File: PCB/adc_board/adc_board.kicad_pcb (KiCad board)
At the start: 4 copper layers, 7 parts, among them U1 MAX6070BAUT33T

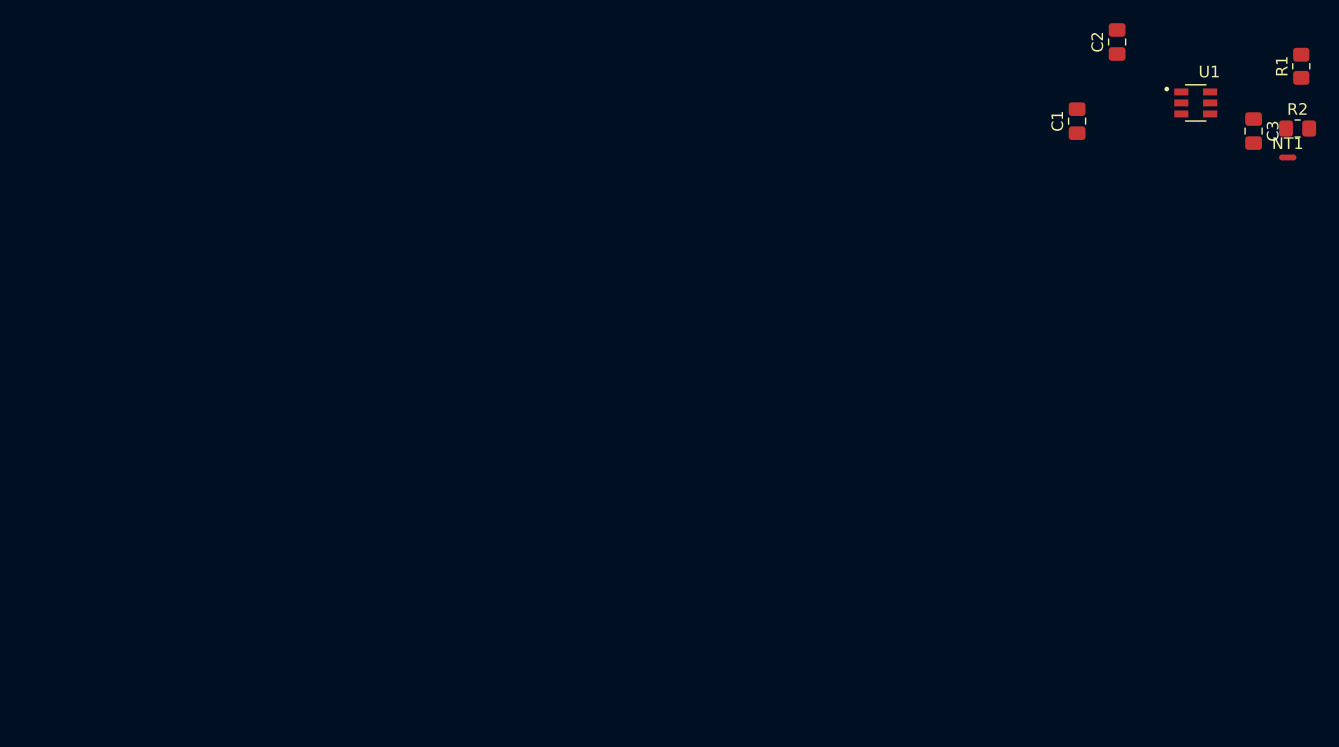
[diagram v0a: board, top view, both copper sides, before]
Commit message: Finished layout for adc board
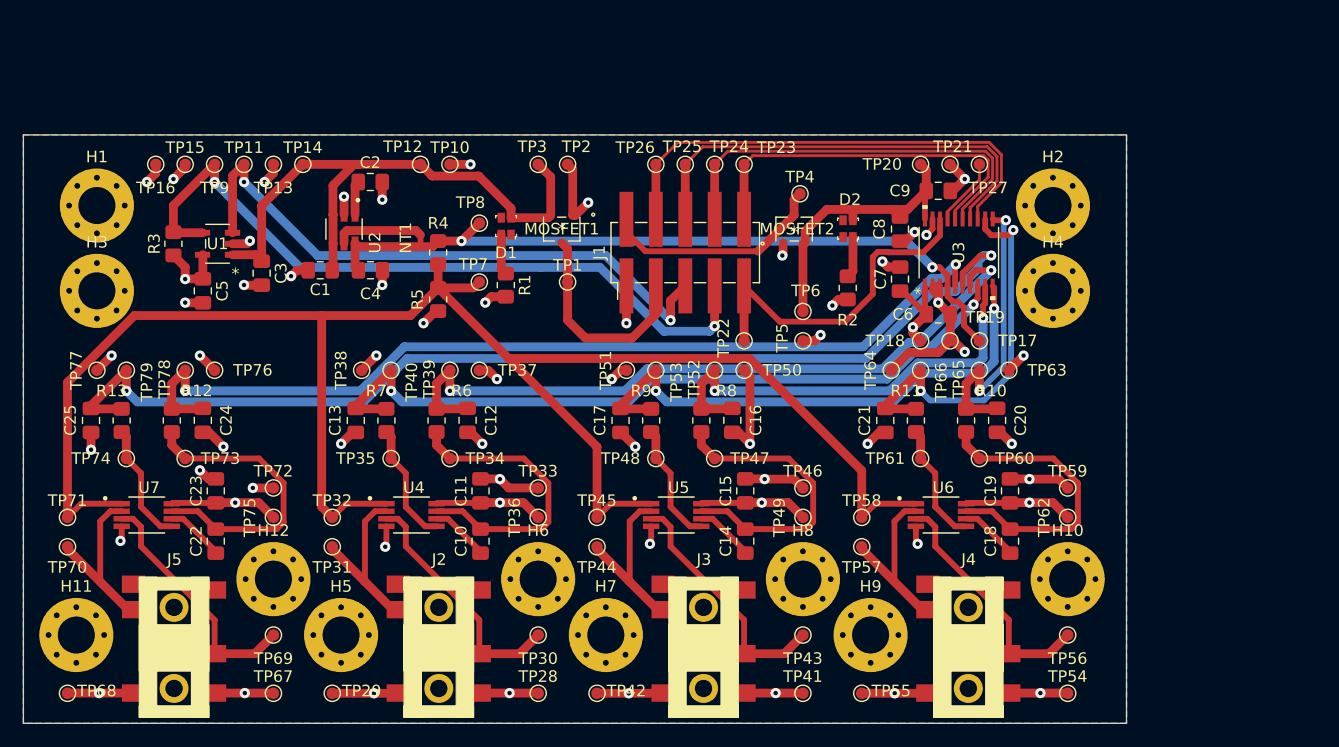
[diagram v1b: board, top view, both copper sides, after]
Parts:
- added C10: 10nF, Capacitor_SMD:C_0805_2012Metric_Pad1.18x1.45mm_HandSolder, F.Cu at (89.0, 124.0)
- added C11: 0.1uF, Capacitor_SMD:C_0805_2012Metric_Pad1.18x1.45mm_HandSolder, F.Cu at (89.0, 119.6)
- added C12: 0.1uF, Capacitor_SMD:C_0805_2012Metric_Pad1.18x1.45mm_HandSolder, F.Cu at (87.9, 113.5)
- added C13: 0.1uF, Capacitor_SMD:C_0805_2012Metric_Pad1.18x1.45mm_HandSolder, F.Cu at (78.2, 113.6)
- added C14: 10nF, Capacitor_SMD:C_0805_2012Metric_Pad1.18x1.45mm_HandSolder, F.Cu at (111.9, 124.0)
- added C15: 0.1uF, Capacitor_SMD:C_0805_2012Metric_Pad1.18x1.45mm_HandSolder, F.Cu at (111.9, 119.6)
- added C16: 0.1uF, Capacitor_SMD:C_0805_2012Metric_Pad1.18x1.45mm_HandSolder, F.Cu at (110.7, 113.5)
- added C17: 0.1uF, Capacitor_SMD:C_0805_2012Metric_Pad1.18x1.45mm_HandSolder, F.Cu at (101.1, 113.6)
- added C18: 10nF, Capacitor_SMD:C_0805_2012Metric_Pad1.18x1.45mm_HandSolder, F.Cu at (134.7, 124.0)
- added C19: 0.1uF, Capacitor_SMD:C_0805_2012Metric_Pad1.18x1.45mm_HandSolder, F.Cu at (134.7, 119.6)
- added C20: 0.1uF, Capacitor_SMD:C_0805_2012Metric_Pad1.18x1.45mm_HandSolder, F.Cu at (133.6, 113.5)
- added C21: 0.1uF, Capacitor_SMD:C_0805_2012Metric_Pad1.18x1.45mm_HandSolder, F.Cu at (124.0, 113.6)
- added C22: 10nF, Capacitor_SMD:C_0805_2012Metric_Pad1.18x1.45mm_HandSolder, F.Cu at (66.1, 124.0)
- added C23: 0.1uF, Capacitor_SMD:C_0805_2012Metric_Pad1.18x1.45mm_HandSolder, F.Cu at (66.1, 119.6)
- added C24: 0.1uF, Capacitor_SMD:C_0805_2012Metric_Pad1.18x1.45mm_HandSolder, F.Cu at (65.0, 113.5)
- added C25: 0.1uF, Capacitor_SMD:C_0805_2012Metric_Pad1.18x1.45mm_HandSolder, F.Cu at (55.4, 113.6)
- added C4: 0.1uF, Capacitor_SMD:C_0805_2012Metric_Pad1.18x1.45mm_HandSolder, F.Cu at (79.5, 100.6)
- added C5: 10uF, Capacitor_SMD:C_0805_2012Metric_Pad1.18x1.45mm_HandSolder, F.Cu at (65.0, 102.4)
- added C6: 0.1uF, Capacitor_SMD:C_0805_2012Metric_Pad1.18x1.45mm_HandSolder, F.Cu at (128.5, 104.4)
- added C7: 10uF, Capacitor_SMD:C_0805_2012Metric_Pad1.18x1.45mm_HandSolder, F.Cu at (125.2, 101.3)
- added C8: 10uF, Capacitor_SMD:C_0805_2012Metric_Pad1.18x1.45mm_HandSolder, F.Cu at (125.2, 97.0)
- added C9: 0.1uF, Capacitor_SMD:C_0805_2012Metric_Pad1.18x1.45mm_HandSolder, F.Cu at (128.5, 93.7)
- added D1: LTST-C19HE1WT, digikey-footprints:LED_Dual0603, F.Cu at (91.2, 96.8)
- added D2: LTST-C19HE1WT, digikey-footprints:LED_Dual0603, F.Cu at (120.7, 97.0)
- added H1: MountingHole, MountingHole:MountingHole_3.2mm_M3_Pad_Via, F.Cu at (55.9, 95.0)
- added H10: MountingHole, MountingHole:MountingHole_3.2mm_M3_Pad_Via, F.Cu at (139.7, 127.3)
- added H11: MountingHole, MountingHole:MountingHole_3.2mm_M3_Pad_Via, F.Cu at (54.1, 132.1)
- added H12: MountingHole, MountingHole:MountingHole_3.2mm_M3_Pad_Via, F.Cu at (71.1, 127.3)
- added H2: MountingHole, MountingHole:MountingHole_3.2mm_M3_Pad_Via, F.Cu at (138.4, 95.0)
- added H3: MountingHole, MountingHole:MountingHole_3.2mm_M3_Pad_Via, F.Cu at (55.9, 102.4)
- added H4: MountingHole, MountingHole:MountingHole_3.2mm_M3_Pad_Via, F.Cu at (138.4, 102.4)
- added H5: MountingHole, MountingHole:MountingHole_3.2mm_M3_Pad_Via, F.Cu at (77.0, 132.1)
- added H6: MountingHole, MountingHole:MountingHole_3.2mm_M3_Pad_Via, F.Cu at (94.0, 127.3)
- added H7: MountingHole, MountingHole:MountingHole_3.2mm_M3_Pad_Via, F.Cu at (99.8, 132.1)
- added H8: MountingHole, MountingHole:MountingHole_3.2mm_M3_Pad_Via, F.Cu at (116.8, 127.3)
- added H9: MountingHole, MountingHole:MountingHole_3.2mm_M3_Pad_Via, F.Cu at (122.7, 132.1)
- added J1: Conn_02x05_Counter_Clockwise, 2x5header:PinHeader_2x05_P2.54mm_Vertical_SMD, F.Cu at (106.7, 99.1)
- added J2: 54-00177, 54-00177:54-00177, F.Cu at (88.9, 139.2)
- added J3: 54-00177, 54-00177:54-00177, F.Cu at (111.8, 139.2)
- added J4: 54-00177, 54-00177:54-00177, F.Cu at (134.6, 139.2)
- added J5: 54-00177, 54-00177:54-00177, F.Cu at (66.0, 139.2)
- added MOSFET1: SSM3J332R, ul_SSM3J332R:SSM3J332R, F.Cu at (96.0, 97.0)
- added MOSFET2: SSM3J332R, ul_SSM3J332R:SSM3J332R, F.Cu at (116.1, 97.0)
- added R10: 100R, Resistor_SMD:R_0805_2012Metric_Pad1.20x1.40mm_HandSolder, F.Cu at (130.9, 113.6)
- added R11: 100R, Resistor_SMD:R_0805_2012Metric_Pad1.20x1.40mm_HandSolder, F.Cu at (126.6, 113.6)
- added R12: 100R, Resistor_SMD:R_0805_2012Metric_Pad1.20x1.40mm_HandSolder, F.Cu at (62.3, 113.6)
- added R13: 100R, Resistor_SMD:R_0805_2012Metric_Pad1.20x1.40mm_HandSolder, F.Cu at (58.0, 113.6)
- added R3: 10K 0.5%, Resistor_SMD:R_0805_2012Metric_Pad1.20x1.40mm_HandSolder, F.Cu at (62.5, 98.3)
- added R4: 10K 0.5%, Resistor_SMD:R_0805_2012Metric_Pad1.20x1.40mm_HandSolder, F.Cu at (85.3, 99.1)
- added R5: 10K 0.5%, Resistor_SMD:R_0805_2012Metric_Pad1.20x1.40mm_HandSolder, F.Cu at (85.3, 103.1)
- added R6: 100R, Resistor_SMD:R_0805_2012Metric_Pad1.20x1.40mm_HandSolder, F.Cu at (85.2, 113.6)
- added R7: 100R, Resistor_SMD:R_0805_2012Metric_Pad1.20x1.40mm_HandSolder, F.Cu at (80.9, 113.6)
- added R8: 100R, Resistor_SMD:R_0805_2012Metric_Pad1.20x1.40mm_HandSolder, F.Cu at (108.1, 113.6)
- added R9: 100R, Resistor_SMD:R_0805_2012Metric_Pad1.20x1.40mm_HandSolder, F.Cu at (103.7, 113.6)
- added TP1: 3V3, TestPoint:TestPoint_Pad_D1.0mm, F.Cu at (96.5, 101.6)
- added TP10: GND, TestPoint:TestPoint_Pad_D1.0mm, F.Cu at (86.4, 91.4)
- added TP11: ENABLE, TestPoint:TestPoint_Pad_D1.0mm, F.Cu at (68.6, 91.4)
- added TP12: 5V_PROT, TestPoint:TestPoint_Pad_D1.0mm, F.Cu at (83.8, 91.4)
- added TP13: GND, TestPoint:TestPoint_Pad_D1.0mm, F.Cu at (71.1, 91.4)
- added TP14: 5V_PROT, TestPoint:TestPoint_Pad_D1.0mm, F.Cu at (73.7, 91.4)
- added TP15: AVDD, TestPoint:TestPoint_Pad_D1.0mm, F.Cu at (63.5, 91.4)
- added TP16: GND, TestPoint:TestPoint_Pad_D1.0mm, F.Cu at (61.0, 91.4)
- added TP17: 3V3_REF, TestPoint:TestPoint_Pad_D1.0mm, F.Cu at (132.1, 106.7)
- added TP18: AVDD, TestPoint:TestPoint_Pad_D1.0mm, F.Cu at (127.0, 106.7)
- added TP19: GND, TestPoint:TestPoint_Pad_D1.0mm, F.Cu at (129.5, 106.7)
- added TP2: GND, TestPoint:TestPoint_Pad_D1.0mm, F.Cu at (96.5, 91.4)
- added TP20: DVDD, TestPoint:TestPoint_Pad_D1.0mm, F.Cu at (127.0, 91.4)
- added TP21: GND, TestPoint:TestPoint_Pad_D1.0mm, F.Cu at (129.5, 91.4)
- added TP22: CLK, TestPoint:TestPoint_Pad_D1.0mm, F.Cu at (111.8, 106.7)
- added TP23: MISO, TestPoint:TestPoint_Pad_D1.0mm, F.Cu at (111.8, 91.4)
- added TP24: MOSI, TestPoint:TestPoint_Pad_D1.0mm, F.Cu at (109.2, 91.4)
- added TP25: SCK, TestPoint:TestPoint_Pad_D1.0mm, F.Cu at (106.7, 91.4)
- added TP26: CS, TestPoint:TestPoint_Pad_D1.0mm, F.Cu at (104.1, 91.4)
- added TP27: IRQ, TestPoint:TestPoint_Pad_D1.0mm, F.Cu at (132.1, 91.4)
- added TP28: VDD, TestPoint:TestPoint_Pad_D1.0mm, F.Cu at (94.0, 137.1)
- added TP29: GND, TestPoint:TestPoint_Pad_D1.0mm, F.Cu at (76.2, 137.1)
- added TP3: 5V_PROT, TestPoint:TestPoint_Pad_D1.0mm, F.Cu at (94.0, 91.4)
- added TP30: BR+, TestPoint:TestPoint_Pad_D1.0mm, F.Cu at (94.0, 132.1)
- added TP31: BR-, TestPoint:TestPoint_Pad_D1.0mm, F.Cu at (76.2, 124.5)
- added TP32: 1V65, TestPoint:TestPoint_Pad_D1.0mm, F.Cu at (76.2, 121.9)
- added TP33: GND, TestPoint:TestPoint_Pad_D1.0mm, F.Cu at (94.0, 119.4)
- added TP34: AMP+, TestPoint:TestPoint_Pad_D1.0mm, F.Cu at (86.4, 116.8)
- added TP35: AMP-, TestPoint:TestPoint_Pad_D1.0mm, F.Cu at (81.3, 116.8)
- added TP36: VDD, TestPoint:TestPoint_Pad_D1.0mm, F.Cu at (94.0, 121.9)
- added TP37: GND, TestPoint:TestPoint_Pad_D1.0mm, F.Cu at (88.9, 109.2)
- added TP38: GND, TestPoint:TestPoint_Pad_D1.0mm, F.Cu at (78.7, 109.2)
- added TP39: DIFF+, TestPoint:TestPoint_Pad_D1.0mm, F.Cu at (86.4, 109.2)
- added TP4: 3V3, TestPoint:TestPoint_Pad_D1.0mm, F.Cu at (116.6, 94.0)
- added TP40: DIFF-, TestPoint:TestPoint_Pad_D1.0mm, F.Cu at (81.3, 109.2)
- added TP41: VDD, TestPoint:TestPoint_Pad_D1.0mm, F.Cu at (116.8, 137.1)
- added TP42: GND, TestPoint:TestPoint_Pad_D1.0mm, F.Cu at (99.1, 137.1)
- added TP43: BR+, TestPoint:TestPoint_Pad_D1.0mm, F.Cu at (116.8, 132.1)
- added TP44: BR-, TestPoint:TestPoint_Pad_D1.0mm, F.Cu at (99.1, 124.5)
- added TP45: 1V65, TestPoint:TestPoint_Pad_D1.0mm, F.Cu at (99.1, 121.9)
- added TP46: GND, TestPoint:TestPoint_Pad_D1.0mm, F.Cu at (116.8, 119.4)
- added TP47: AMP+, TestPoint:TestPoint_Pad_D1.0mm, F.Cu at (109.2, 116.8)
- added TP48: AMP-, TestPoint:TestPoint_Pad_D1.0mm, F.Cu at (104.1, 116.8)
- added TP49: VDD, TestPoint:TestPoint_Pad_D1.0mm, F.Cu at (116.8, 121.9)
- added TP5: GND, TestPoint:TestPoint_Pad_D1.0mm, F.Cu at (116.8, 106.7)
- added TP50: GND, TestPoint:TestPoint_Pad_D1.0mm, F.Cu at (111.8, 109.2)
- added TP51: GND, TestPoint:TestPoint_Pad_D1.0mm, F.Cu at (101.6, 109.2)
- added TP52: DIFF+, TestPoint:TestPoint_Pad_D1.0mm, F.Cu at (109.2, 109.2)
- added TP53: DIFF-, TestPoint:TestPoint_Pad_D1.0mm, F.Cu at (104.1, 109.2)
- added TP54: VDD, TestPoint:TestPoint_Pad_D1.0mm, F.Cu at (139.7, 137.1)
- added TP55: GND, TestPoint:TestPoint_Pad_D1.0mm, F.Cu at (121.9, 137.1)
- added TP56: BR+, TestPoint:TestPoint_Pad_D1.0mm, F.Cu at (139.7, 132.1)
- added TP57: BR-, TestPoint:TestPoint_Pad_D1.0mm, F.Cu at (121.9, 124.5)
- added TP58: 1V65, TestPoint:TestPoint_Pad_D1.0mm, F.Cu at (121.9, 121.9)
- added TP59: GND, TestPoint:TestPoint_Pad_D1.0mm, F.Cu at (139.7, 119.4)
- added TP6: 3V3_PROT, TestPoint:TestPoint_Pad_D1.0mm, F.Cu at (116.8, 104.1)
- added TP60: AMP+, TestPoint:TestPoint_Pad_D1.0mm, F.Cu at (132.1, 116.8)
- added TP61: AMP-, TestPoint:TestPoint_Pad_D1.0mm, F.Cu at (127.0, 116.8)
- added TP62: VDD, TestPoint:TestPoint_Pad_D1.0mm, F.Cu at (139.7, 121.9)
- added TP63: GND, TestPoint:TestPoint_Pad_D1.0mm, F.Cu at (134.6, 109.2)
- added TP64: GND, TestPoint:TestPoint_Pad_D1.0mm, F.Cu at (124.5, 109.2)
- added TP65: DIFF+, TestPoint:TestPoint_Pad_D1.0mm, F.Cu at (132.1, 109.2)
- added TP66: DIFF-, TestPoint:TestPoint_Pad_D1.0mm, F.Cu at (127.0, 109.2)
- added TP67: VDD, TestPoint:TestPoint_Pad_D1.0mm, F.Cu at (71.1, 137.1)
- added TP68: GND, TestPoint:TestPoint_Pad_D1.0mm, F.Cu at (53.3, 137.1)
- added TP69: BR+, TestPoint:TestPoint_Pad_D1.0mm, F.Cu at (71.1, 132.1)
- added TP7: 1V65_REF, TestPoint:TestPoint_Pad_D1.0mm, F.Cu at (88.9, 101.6)
- added TP70: BR-, TestPoint:TestPoint_Pad_D1.0mm, F.Cu at (53.3, 124.5)
- added TP71: 1V65, TestPoint:TestPoint_Pad_D1.0mm, F.Cu at (53.3, 121.9)
- added TP72: GND, TestPoint:TestPoint_Pad_D1.0mm, F.Cu at (71.1, 119.4)
- added TP73: AMP+, TestPoint:TestPoint_Pad_D1.0mm, F.Cu at (63.5, 116.8)
- added TP74: AMP-, TestPoint:TestPoint_Pad_D1.0mm, F.Cu at (58.4, 116.8)
- added TP75: VDD, TestPoint:TestPoint_Pad_D1.0mm, F.Cu at (71.1, 121.9)
- added TP76: GND, TestPoint:TestPoint_Pad_D1.0mm, F.Cu at (66.0, 109.2)
- added TP77: GND, TestPoint:TestPoint_Pad_D1.0mm, F.Cu at (55.9, 109.2)
- added TP78: DIFF+, TestPoint:TestPoint_Pad_D1.0mm, F.Cu at (63.5, 109.2)
- added TP79: DIFF-, TestPoint:TestPoint_Pad_D1.0mm, F.Cu at (58.4, 109.2)
- added TP8: 3V3_REF, TestPoint:TestPoint_Pad_D1.0mm, F.Cu at (88.9, 96.5)
- added TP9: PGOOD, TestPoint:TestPoint_Pad_D1.0mm, F.Cu at (66.0, 91.4)
- added U2: MAX6070BAUT33T, MAX6070BAUT33T:SOT95P280X145-6N, F.Cu at (77.2, 97.0)
- added U3: MCP3564-E_ST, ‎MCP3564-E-ST:MCP3564-E&slash_ST, F.Cu at (130.3, 99.1)
- added U4: MAX4209HAUA, MAX4209HAUA:SOP65P490X110-8N, F.Cu at (83.0, 121.7)
- added U5: MAX4209HAUA, MAX4209HAUA:SOP65P490X110-8N, F.Cu at (105.9, 121.7)
- added U6: MAX4209HAUA, MAX4209HAUA:SOP65P490X110-8N, F.Cu at (128.8, 121.7)
- added U7: MAX4209HAUA, MAX4209HAUA:SOP65P490X110-8N, F.Cu at (60.2, 121.7)
- C3: value 0.1uF -> 10uF
- R1, R2: value 10K -> 100R
- U1: value MAX6070BAUT33T -> MCP1755T-3302E_OT; footprint MAX6070BAUT33T:SOT95P280X145-6N -> ul_MCP1755T-3302E-OT:MCP1755T-3302E&slash_OT
- moved C3 86.5 mm to (70.1, 100.8)
- moved U1 85.3 mm to (66.3, 98.3), turned to 180 degrees
- moved NT1 75.2 mm to (83.8, 98.0), turned to 270 degrees
- moved R1 71.2 mm to (91.2, 101.9), turned to 270 degrees
- moved C1 66.6 mm to (75.2, 100.6), turned to 180 degrees
- moved C2 65.6 mm to (79.5, 93.0), turned to 0 degrees
- moved R2 41.2 mm to (120.7, 102.1), turned to 270 degrees
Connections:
- C1 pad 1: +5V -> /3V3_REF_VIN
- C3 pad 1: /3V3_REF_OUT -> /3V3_REF_VIN
- R1 pad 1: /3V3_REF_OUT -> Net-(D1-Pad2)
- R1 pad 2: /1V65_REF -> GND
- R2 pad 1: /1V65_REF -> Net-(D2-Pad1)
- U1 pad 1: /3V3_REF_FILTER -> /3V3_REF_VIN
- U1 pad 3: +5V -> /ENABLE
- U1 pad 4: +5V -> /PGOOD
- U1 pad 5: /3V3_REF_OUTS -> /ADC_AVDD
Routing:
- net GND: track 0.00 -> 479.2 mm, vias 0 -> 50
- net /ADC_AVDD: track 0.00 -> 287.9 mm, vias 0 -> 11
- net /1V65_REF: track 0.00 -> 155.3 mm
- net /Sheet61550FD4/ADC_CH1: track 0.00 -> 94.0 mm, vias 0 -> 2
- net /Sheet61550FD4/ADC_CH0: track 0.00 -> 81.4 mm, vias 0 -> 2
- net /3V3_REF_OUT: track 0.00 -> 65.0 mm, vias 0 -> 2
- net /Sheet61550FD4/ADC_CH3: track 0.00 -> 64.9 mm, vias 0 -> 2
- net /PGOOD: track 0.00 -> 63.6 mm, vias 0 -> 2
- net /Sheet61550FD4/ADC_CH2: track 0.00 -> 62.3 mm, vias 0 -> 2
- net /ENABLE: track 0.00 -> 53.1 mm, vias 0 -> 2
- net /3V3_REF_VIN: track 0.00 -> 51.2 mm
- net /Sheet61550FD4/ADC_CH5: track 0.00 -> 46.6 mm, vias 0 -> 2
- net /CS: track 0.00 -> 42.2 mm
- net /SCK: track 0.00 -> 39.0 mm
- net /Sheet61550FD4/ADC_CH4: track 0.00 -> 38.9 mm, vias 0 -> 2
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- added copper zone on B.Cu, net (none)
- added copper zone on F.Cu, net (none)
- added copper zone on In2.Cu, net /ADC_AVDD
- added copper zone on In1.Cu, net GND
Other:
- board outline added: 95.2 x 50.8 mm

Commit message: whatever the latest changes were
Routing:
- net GND: track 479.2 -> 146.1 mm
- net /ADC_AVDD: track 287.9 -> 74.3 mm
